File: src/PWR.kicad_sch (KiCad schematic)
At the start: 59 parts, among them J1 USB_C_Receptacle_USB2.0_16P, Q1 AO3401A, Q11 SI2308A, Q12 SI2308A, Q13 SI2308A, Q2 AO3401A, U14 TPS54302DDCR, U19 TPS54302DDCR, U4 TPS54302DDCR

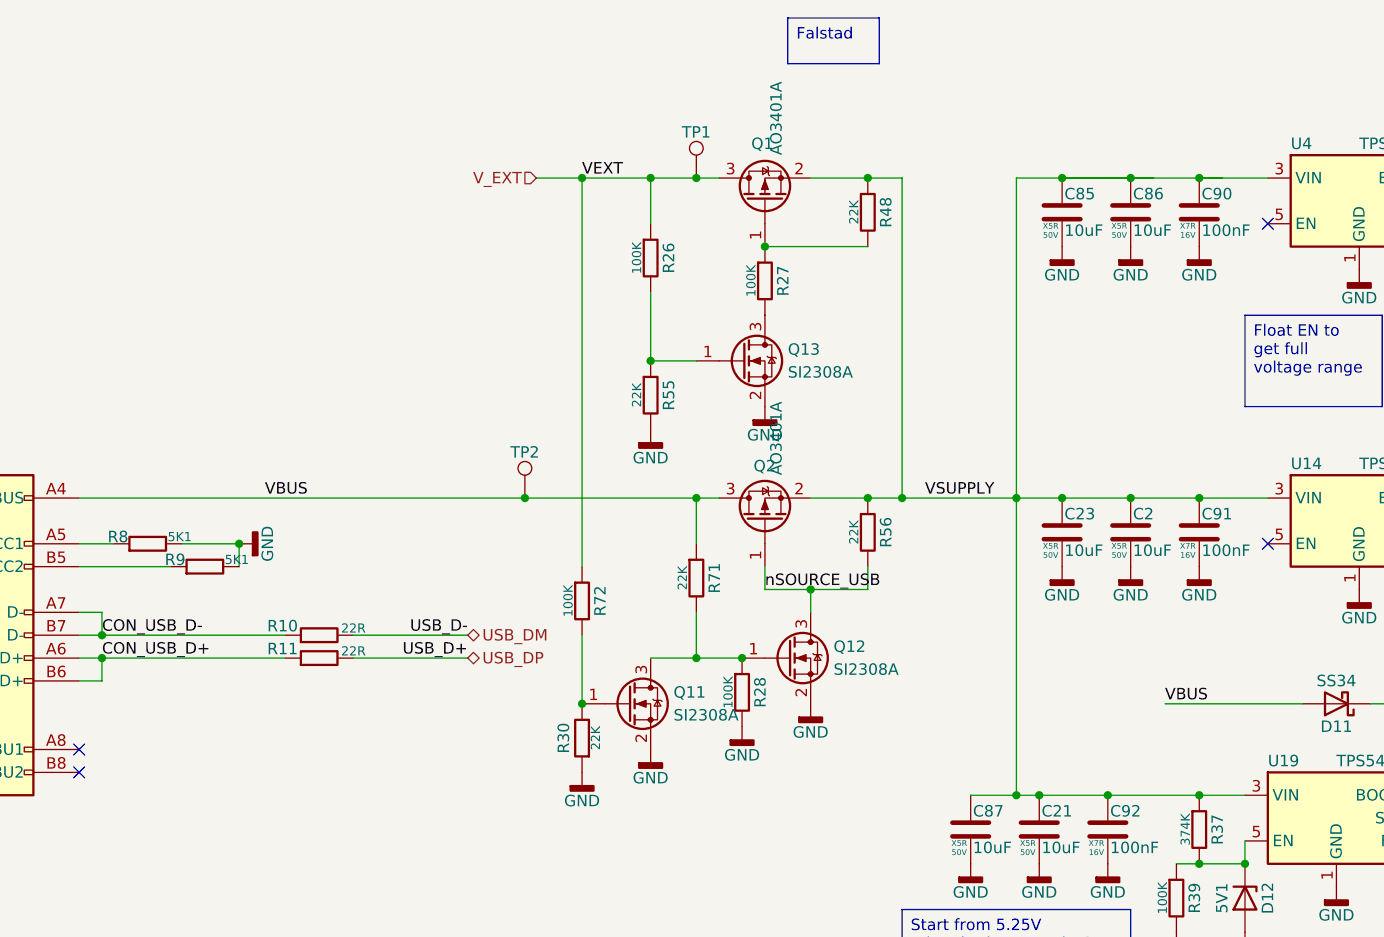
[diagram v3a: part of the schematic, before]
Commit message: schematic cleanup, verification. GPIO9 pin pulldown changed to pullup.
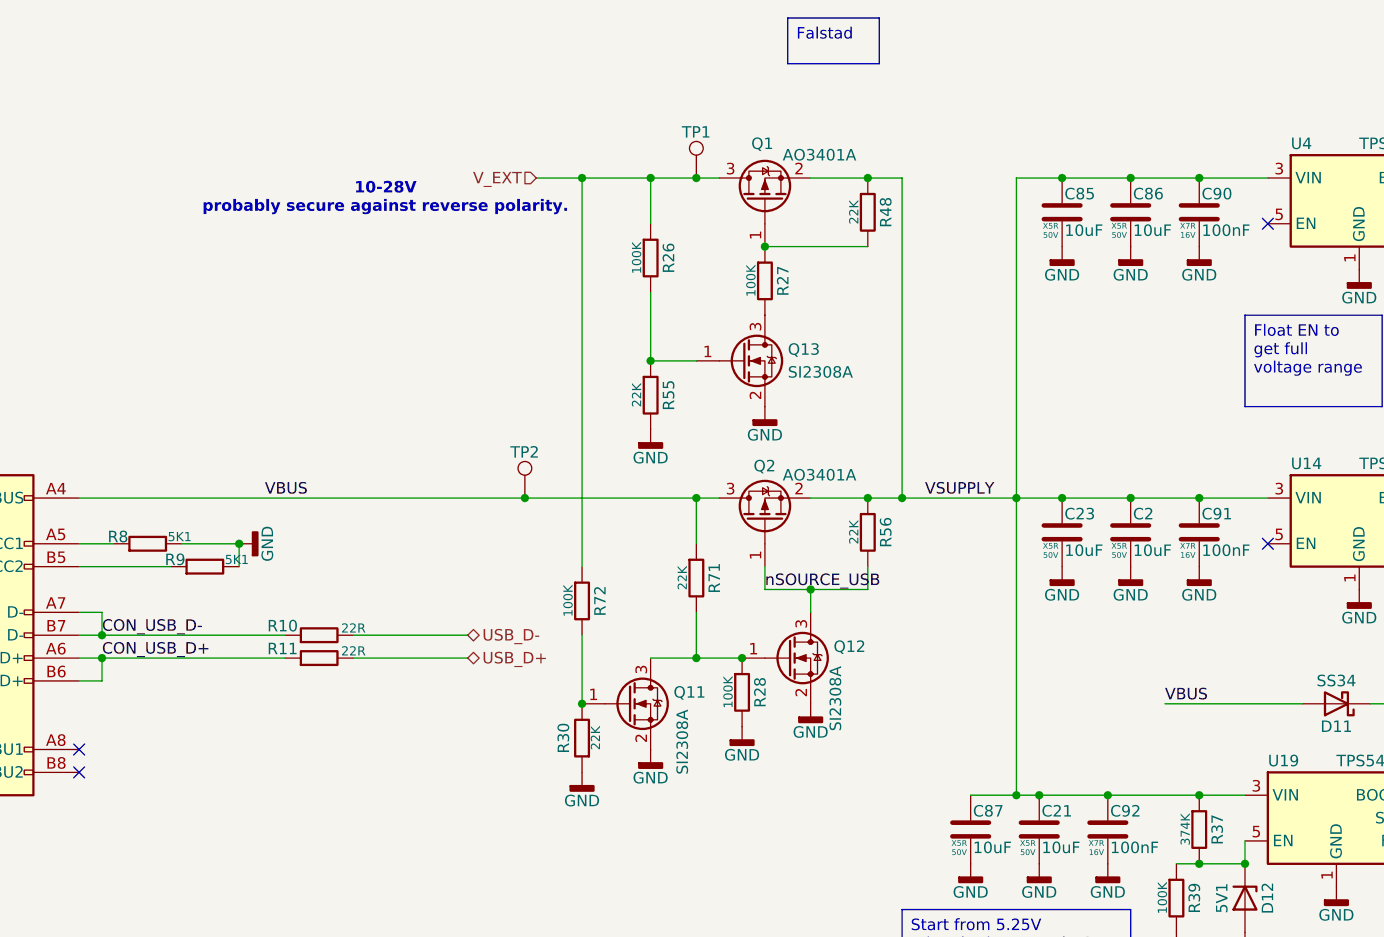
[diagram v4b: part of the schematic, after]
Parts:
- R37: Supplier Part Number 1 C44358 -> C25781
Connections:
- net USB_DM renamed USB_D-
- net USB_DP renamed USB_D+
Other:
- note added: "10-28V probably secure against reverse polarity."
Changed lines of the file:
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@@
 	(generator_version "10.0")
 	(paper "A4")
+	(text "10-28V\nprobably secure against reverse polarity."
+		(exclude_from_sim no)
+		(at 79.756 37.846 0)
+		(effects
+			(font
+				(size 1.27 1.27)
+				(thickness 0.254)
+				(bold yes)
+			)
+		)
+	)
 	(text "DISABLE WHEN EXT. voltage applied (higher than USB)"
 		(exclude_from_sim no)
@@
 	)
 	(junction
+		(at 162.56 35.56)
+		(diameter 0)
+		(color 0 0 0 0)
+	)
+	(junction
 		(at 133.35 71.12)
 		(diameter 0)
@@
 	)
 	(junction
-		(at 154.94 35.56)
-		(diameter 0)
-		(color 0 0 0 0)
-	)
-	(junction
-		(at 170.18 35.56)
-		(diameter 0)
-		(color 0 0 0 0)
-	)
-	(junction
 		(at 248.92 106.68)
 		(diameter 0)
@@
 	)
 	(junction
+		(at 154.94 35.56)
+		(diameter 0)
+		(color 0 0 0 0)
+	)
+	(junction
 		(at 154.94 71.12)
 		(diameter 0)
@@
 	)
 	(junction
-		(at 162.56 35.56)
-		(diameter 0)
-		(color 0 0 0 0)
-	)
-	(junction
 		(at 109.22 35.56)
 		(diameter 0)
@@
 	)
 	(junction
+		(at 170.18 35.56)
+		(diameter 0)
+		(color 0 0 0 0)
+	)
+	(junction
 		(at 231.14 45.72)
 		(diameter 0)
@@
 	(wire
 		(pts
-			(xy 162.56 35.56) (xy 165.1 35.56)
-		)
-		(stroke
-			(width 0)
-			(type default)
-		)
-	)
-	(wire
-		(pts
 			(xy 149.86 71.12) (xy 149.86 35.56)
 		)
@@
 	(wire
 		(pts
-			(xy 149.86 35.56) (xy 154.94 35.56)
-		)
-		(stroke
-			(width 0.508)
-			(type default)
-			(color 255 0 255 1)
-		)
-	)
-	(wire
-		(pts
 			(xy 149.86 104.14) (xy 149.86 71.12)
 		)
@@
 	(wire
 		(pts
-			(xy 154.94 35.56) (xy 162.56 35.56)
+			(xy 149.86 35.56) (xy 154.94 35.56)
 		)
 		(stroke
@@
 	(wire
 		(pts
-			(xy 200.66 104.14) (xy 200.66 99.06)
+			(xy 154.94 35.56) (xy 162.56 35.56)
 		)
 		(stroke
-			(width 0)
+			(width 0.508)
 			(type default)
+			(color 255 0 255 1)
 		)
 	)
 	(wire
 		(pts
-			(xy 121.92 78.74) (xy 121.92 81.28)
+			(xy 200.66 104.14) (xy 200.66 99.06)
 		)
 		(stroke
@@
 	(wire
 		(pts
-			(xy 231.14 45.72) (xy 241.3 45.72)
+			(xy 121.92 78.74) (xy 121.92 81.28)
 		)
 		(stroke
@@
 	(wire
 		(pts
-			(xy 114.3 71.12) (xy 116.84 71.12)
+			(xy 231.14 45.72) (xy 241.3 45.72)
 		)
 		(stroke
-			(width 0.508)
+			(width 0)
 			(type default)
-			(color 255 0 0 1)
 		)
 	)
 	(wire
 		(pts
-			(xy 170.18 35.56) (xy 172.72 35.56)
+			(xy 114.3 71.12) (xy 116.84 71.12)
 		)
 		(stroke
-			(width 0)
+			(width 0.508)
 			(type default)
+			(color 255 0 0 1)
 		)
 	)
 	(wire
 		(pts
-			(xy 154.94 35.56) (xy 162.56 35.56)
+			(xy 162.56 35.56) (xy 170.18 35.56)
 		)
 		(stroke
-			(width 0)
+			(width 0.508)
 			(type default)
+			(color 255 0 255 1)
 		)
 	)
@@
 		)
 	)
-	(wire
-		(pts
-			(xy 162.56 35.56) (xy 170.18 35.56)
-		)
-		(stroke
-			(width 0.508)
-			(type default)
-			(color 255 0 255 1)
-		)
-	)
 	(label "VSUPPLY"
 		(at 139.7 71.12 0)
@@
 		)
 	)
-	(label "USB_D+"
-		(at 88.9 88.9 180)
-		(effects
-			(font
-				(size 1.27 1.27)
-			)
-			(justify right bottom)
-		)
-	)
-	(label "VEXT"
-		(at 101.6 35.56 0)
-		(effects
-			(font
-				(size 1.27 1.27)
-			)
-			(justify left bottom)
-		)
-	)
-	(label "USB_D-"
-		(at 88.9 86.36 180)
-		(effects
-			(font
-				(size 1.27 1.27)
-			)
-			(justify right bottom)
-		)
-	)
 	(label "VBUS"
 		(at 166.37 93.98 0)
@@
 		)
 	)
-	(hierarchical_label "USB_DP"
+	(hierarchical_label "USB_D+"
 		(shape tri_state)
 		(at 88.9 88.9 0)
@@
 		)
 	)
-	(hierarchical_label "USB_DM"
+	(hierarchical_label "USB_D-"
 		(shape tri_state)
 		(at 88.9 86.36 0)
@@
 		)
 		(property "Value" "SI2308A"
-			(at 111.76 95.25 0)
+			(at 112.776 101.854 90)
 			(show_name no)
 			(do_not_autoplace no)
@@
 			)
 		)
-		(property "Manufacturer" ""
-			(at 95.25 71.12 0)
-			(hide yes)
-			(show_name no)
-			(do_not_autoplace no)
-			(effects
-				(font
-					(size 1.27 1.27)
-				)
-			)
-		)
-		(property "Manufacturer Part Number" ""
+		(property "Supplier 1" ""
 			(at 95.25 71.12 0)
 			(hide yes)
@@
 			(effects
 				(font
-					(size 1.27 1.27)
+					(size 1 1)
 				)
 			)
 		)
-		(property "on_board" ""
+		(property "Supplier Part Number 1" ""
 			(at 95.25 71.12 0)
 			(hide yes)
@@
 			(effects
 				(font
-					(size 1.27 1.27)
+					(size 1 1)
 				)
 			)
@@
 		)
 		(property "Value" "AO3401A"
-			(at 123.19 68.58 0)
+			(at 132.08 68.58 90)
 			(show_name no)
 			(do_not_autoplace no)
@@
 		)
 		(property "Value" "AO3401A"
-			(at 123.19 33.02 0)
+			(at 132.08 33.02 90)
 			(show_name no)
 			(do_not_autoplace no)
@@
 			)
 		)
-		(property "Supplier Part Number 1" "C44358"
+		(property "Supplier Part Number 1" "C25781"
 			(at 170.18 107.95 0)
 			(hide yes)
@@
 			)
 		)
-		(property "Manufacturer" ""
-			(at 170.18 107.95 90)
-			(hide yes)
-			(show_name no)
-			(do_not_autoplace no)
-			(effects
-				(font
-					(size 1.27 1.27)
-				)
-			)
-		)
-		(property "Manufacturer Part Number" ""
-			(at 170.18 107.95 90)
-			(hide yes)
-			(show_name no)
-			(do_not_autoplace no)
-			(effects
-				(font
-					(size 1.27 1.27)
-				)
-			)
-		)
-		(property "on_board" ""
-			(at 170.18 107.95 90)
-			(hide yes)
-			(show_name no)
-			(do_not_autoplace no)
-			(effects
-				(font
-					(size 1.27 1.27)
-				)
-			)
-		)
 		(pin "1"
 		)
@@
 		)
 		(property "Value" "SI2308A"
-			(at 129.54 90.17 0)
+			(at 129.794 97.028 90)
 			(show_name no)
 			(do_not_autoplace no)
@@
 			)
 		)
-		(property "Manufacturer" ""
+		(property "Supplier 1" ""
 			(at 114.3 35.56 0)
 			(hide yes)
@@
 			(effects
 				(font
-					(size 1.27 1.27)
-				)
-			)
-		)
-		(property "Manufacturer Part Number" ""
-			(at 114.3 35.56 0)
-			(hide yes)
-			(show_name no)
-			(do_not_autoplace no)
-			(effects
-				(font
-					(size 1.27 1.27)
+					(size 1 1)
 				)
 			)
 		)
-		(property "on_board" ""
+		(property "Supplier Part Number 1" ""
 			(at 114.3 35.56 0)
 			(hide yes)
@@
 			(effects
 				(font
-					(size 1.27 1.27)
+					(size 1 1)
 				)
 			)
